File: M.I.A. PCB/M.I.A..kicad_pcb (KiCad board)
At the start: 2 copper layers, 50.8 x 101.6 mm, 118 parts, among them J1 USB_C_Receptacle_USB2.0_16P, J10 Conn_01x03, J11 Conn_01x03, J12 Conn_Coaxial, J2 Conn_01x02_Pin, J3 Conn_01x03, J4 Conn_01x03, J5 Conn_01x03, J6 Conn_01x03, J7 MSD-4-A, J8 Conn_01x03, J9 Conn_01x03, SW1 SW_Push, SW2 SW_Push, U1 W25Q128JVS, U10 INA226, U11 AMS1117-3.3, U12 AP62150WU, U13 TPS2121RUXR, U14 AP62150WU, U15 74AHC541, U16 RFM95W-915S2, U2 RP2350B-QFN80, U3 MMC5983MA, U4 ICM-42688-P, U5 MS5611-01BA, U6 TMP117xxDRV, U7 MAX-M10S, U8 KX134-1211, U9 TPS2121RUXR, Y1 ABM8-272-T3

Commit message: Started Layout
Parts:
- J7, U7: moved to B.Cu
- moved SW1 156.9 mm to (-26.5, 86.4)
- moved SW2 147.1 mm to (-16.6, 86.4)
- moved 1.1V1 138.7 mm to (3.75, 19.6)
- moved U13 106.4 mm to (36.9, 91.2)
- moved U14 98.9 mm to (36.7, 99.6)
- moved J7 98.1 mm to (-12.8, 50.6), turned to 90 degrees
- moved U5 96.5 mm to (45.5, 54.0)
- moved C24 94.7 mm to (45.5, 50.2)
- moved U9 86.1 mm to (54.3, 91.2)
- moved U12 85.6 mm to (54.1, 99.7)
- moved R1 78.0 mm to (48.1, 82.1), turned to 135 degrees
- moved C14 75.5 mm to (45.9, 80.0), turned to 135 degrees
- moved L1 75.2 mm to (49.8, 80.2), turned to -135 degrees
- moved C15 74.0 mm to (47.5, 77.8), turned to -135 degrees
- moved Y1 73.3 mm to (-15.1, 101.3), turned to 180 degrees
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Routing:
- net /QSPI_SD1: track 0.00 -> 15.7 mm, vias 0 -> 2
- net Net-(J1-CC1): track 0.00 -> 15.1 mm
- net /QSPI_SD2: track 0.00 -> 15.0 mm
- net /QSPI_SS: track 0.00 -> 14.4 mm, vias 0 -> 2
- net /D-: track 0.00 -> 11.9 mm
- net /D+: track 0.00 -> 10.8 mm
- net /USB-: track 0.00 -> 9.41 mm
- net /USB+: track 0.00 -> 8.56 mm
- net /QSPI_SD0: track 0.00 -> 8.42 mm
- net +3.3V: track 0.00 -> 7.91 mm
- net /QSPI_SCLK: track 0.00 -> 7.89 mm
- net /QSPI_SD3: track 0.00 -> 7.37 mm
- net Net-(J1-CC2): track 0.00 -> 5.99 mm
- net Net-(U2-VREG_AVDD): track 0.00 -> 5.54 mm
- net Net-(U2-VREG_LX): track 0.00 -> 5.39 mm
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- added copper zone on In1.Cu, net GND
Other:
- outline, holes or cut-outs redrawn
- copper layers 2 -> 4

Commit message: Worked on Layout, Changed IMU
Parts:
- added C14: 4.7u, Capacitor_SMD:C_0603_1608Metric, F.Cu at (89.4, 124.8)
- added C15: 4.7u, Capacitor_SMD:C_0603_1608Metric, F.Cu at (89.4, 127.3)
- added C20: 100n, Capacitor_SMD:C_0603_1608Metric, F.Cu at (79.8, 42.0)
- added C21: 100n, Capacitor_SMD:C_0603_1608Metric, F.Cu at (79.8, 44.5)
- added D3: BZT52Bxx, Diode_SMD:D_SOD-123F, F.Cu at (-0.05, 115.9)
- added D4: BZT52Bxx, Diode_SMD:D_SOD-123F, F.Cu at (-0.05, 119.3)
- added D5: BZT52Bxx, Diode_SMD:D_SOD-123F, B.Cu at (-17.7, 114.9)
- added D6: BZT52Bxx, Diode_SMD:D_SOD-123F, F.Cu at (-0.05, 126.0)
- added F1: ERBRE3R00V, JLCImport:ERBRE3R00V, F.Cu at (-0.85, 128.9)
- added F2: ERBRE3R00V, JLCImport:ERBRE3R00V, F.Cu at (-0.85, 131.3)
- added F3: ERBRE3R00V, JLCImport:ERBRE3R00V, F.Cu at (-22.3, 107.9)
- added F4: ERBRE3R00V, JLCImport:ERBRE3R00V, F.Cu at (-0.85, 136.1)
- added J13: Screw_Terminal_01x02, TerminalBlock_Phoenix:TerminalBlock_Phoenix_MKDS-1-2-3.81_1x02_P3.81mm_Horizontal, F.Cu at (67.0, 90.8)
- added J14: Screw_Terminal_01x02, TerminalBlock_Phoenix:TerminalBlock_Phoenix_MKDS-1-2-3.81_1x02_P3.81mm_Horizontal, F.Cu at (67.0, 106.0)
- added J15: Screw_Terminal_01x02, TerminalBlock_Phoenix:TerminalBlock_Phoenix_MKDS-1-2-3.81_1x02_P3.81mm_Horizontal, F.Cu at (67.0, 98.4)
- added J16: Screw_Terminal_01x02, TerminalBlock_Phoenix:TerminalBlock_Phoenix_MKDS-1-2-3.81_1x02_P3.81mm_Horizontal, F.Cu at (24.7, 81.0)
- added J17: Screw_Terminal_01x02, TerminalBlock_Phoenix:TerminalBlock_Phoenix_MKDS-1-2-3.81_1x02_P3.81mm_Horizontal, F.Cu at (24.7, 91.0)
- added J18: Screw_Terminal_01x02, TerminalBlock_Phoenix:TerminalBlock_Phoenix_MKDS-1-2-3.81_1x02_P3.81mm_Horizontal, F.Cu at (24.7, 101.0)
- added Q1: AO3400A, Package_TO_SOT_SMD:SOT-23, F.Cu at (-5.28, 116.7)
- added Q2: AO3400A, Package_TO_SOT_SMD:SOT-23, F.Cu at (-5.28, 121.3)
- added Q3: AO3400A, Package_TO_SOT_SMD:SOT-23, F.Cu at (-20.6, 114.7)
- added Q4: AO3400A, Package_TO_SOT_SMD:SOT-23, F.Cu at (-5.28, 130.5)
- added R1: 33, Resistor_SMD:R_0603_1608Metric, F.Cu at (89.4, 132.3)
- added R34: 1k, Resistor_SMD:R_0603_1608Metric, F.Cu at (-5.72, 100.5)
- added R35: 10k, Resistor_SMD:R_0603_1608Metric, F.Cu at (-5.72, 103.0)
- added R36: 5M, Resistor_SMD:R_0603_1608Metric, F.Cu at (-5.72, 105.5)
- added R37: 1M, Resistor_SMD:R_0603_1608Metric, F.Cu at (-5.72, 108.0)
- added R38: 5M, Resistor_SMD:R_0603_1608Metric, F.Cu at (-5.72, 110.5)
- added R39: 1k, Resistor_SMD:R_0603_1608Metric, F.Cu at (-5.72, 113.0)
- added R40: 10k, Resistor_SMD:R_0603_1608Metric, F.Cu at (-1.72, 100.5)
- added R41: 1M, Resistor_SMD:R_0603_1608Metric, F.Cu at (-1.72, 103.0)
- added R42: 5M, Resistor_SMD:R_0603_1608Metric, B.Cu at (-20.6, 117.9)
- added R43: 1k, Resistor_SMD:R_0603_1608Metric, B.Cu at (-17.5, 111.9)
- added R44: 10k, Resistor_SMD:R_0603_1608Metric, B.Cu at (-20.5, 111.9)
- added R45: 1M, Resistor_SMD:R_0603_1608Metric, B.Cu at (-17.6, 117.9)
- added R46: 5M, Resistor_SMD:R_0603_1608Metric, F.Cu at (2.29, 100.5)
- added R47: 1k, Resistor_SMD:R_0603_1608Metric, F.Cu at (2.29, 103.0)
- added R48: 10k, Resistor_SMD:R_0603_1608Metric, F.Cu at (2.29, 105.5)
- added R49: 1M, Resistor_SMD:R_0603_1608Metric, F.Cu at (2.29, 108.0)
- added REF**: 3x4PinHeaderCase, 3x4DupontCasing:3x4PinHeaderCase, F.Cu at (62.0, 116.5)
- added REF**: 3x4PinHeaderCase, 3x4DupontCasing:3x4PinHeaderCase, F.Cu at (28.8, 116.5)
- C28, C31, C32, C33, C34, C35, C36, C37, D1, D2, L2, L3, R11, R12, R13, R14, R15, R17, R18, R19, R20, R21, R22, R23, R24, R25, R26, R27, U12, U13, U14, U9: moved to B.Cu
- U4: value ICM-42688-P -> ICM-45686; footprint Package_LGA:LGA-14_3x2.5mm_P0.5mm_LayoutBorder3x4y -> Package_LGA:Bosch_LGA-14_3x2.5mm_P0.5mm
- moved C38 175.3 mm to (-35.2, 75.6)
- moved C39 175.3 mm to (-30.9, 85.3)
- moved R28 175.3 mm to (-35.2, 80.7)
- moved R29 175.3 mm to (-35.2, 83.2)
- moved R30 175.3 mm to (-35.2, 85.7)
- moved R31 175.3 mm to (-35.2, 88.2)
- moved R32 175.3 mm to (-35.2, 90.7)
- moved R33 175.3 mm to (-35.2, 93.2)
- moved 3v1 141.0 mm to (1.02, 1.02)
- moved 3v2 141.0 mm to (1.02, 4.08)
- moved USB_3.1 141.0 mm to (1.02, 7.12)
- moved C29 121.7 mm to (-6.85, 72.6)
- moved C30 121.7 mm to (-6.85, 75.6)
- moved R10 108.7 mm to (20.8, 71.6)
- moved R9 108.7 mm to (20.8, 69.0)
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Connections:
- U4 pad 10: +3.3V -> unconnected-(U4-RESV/AUX1_CS-Pad10)
- U4 pad 2: +3.3V -> unconnected-(U4-RESV/AUX1_SDIO/AUX1_SDI/MAS_DA-Pad2)
- U4 pad 3: +3.3V -> unconnected-(U4-RESV/AUX1_SCLK/MAS_CLK-Pad3)
- U4 pad 5: +3.3V -> Net-(U4-VDDIO)
- U4 pad 7: GND -> unconnected-(U4-RESV-Pad7)
- U4 pad 8: +3.3V -> Net-(U4-VDD)
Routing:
- net +3.3V: track 7.91 -> 66.5 mm, vias 0 -> 8
- net +1V1: track 0.82 -> 17.6 mm, vias 1 -> 2
- net Net-(U2-XIN): track 0.00 -> 12.5 mm
- net GND: track 3.20 -> 12.8 mm, vias 7 -> 11
- net Net-(U2-XOUT): track 0.00 -> 7.61 mm
- net Net-(C19-Pad2): track 0.00 -> 3.64 mm
- net unconnected-(U2-GPIO1-Pad78): track 0.00 -> 1.87 mm, vias 0 -> 1
- net unconnected-(U2-GPIO0-Pad77): track 0.00 -> 1.39 mm, vias 0 -> 1
- net unconnected-(U2-GPIO2-Pad79): track 0.00 -> 1.39 mm, vias 0 -> 1
- net unconnected-(U2-GPIO3-Pad80): track 0.00 -> 0.37 mm, vias 0 -> 1
- added copper zone on In2.Cu, net +3.3V
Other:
- board size 50.8 x 101.6 mm -> 50.8 x 106.6 mm
- copper layers 4 -> 6
- board text added: "|\/||/\"

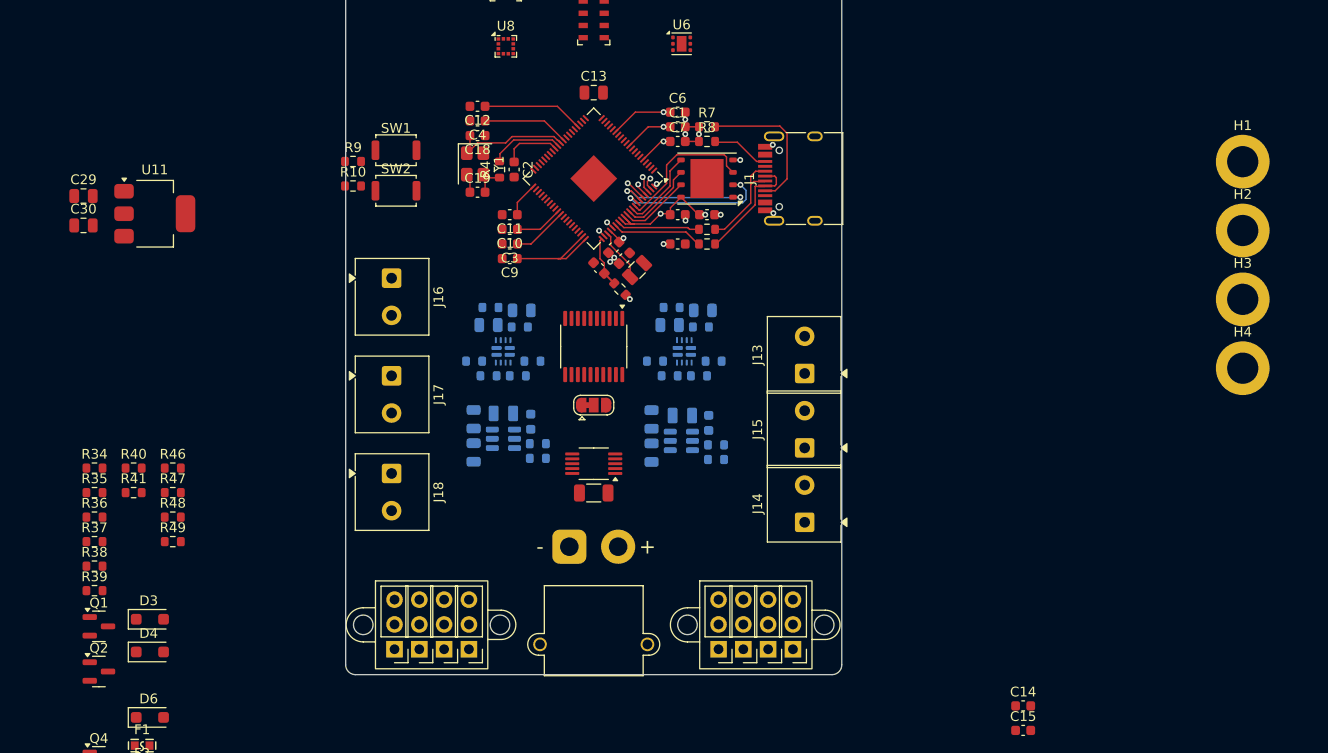
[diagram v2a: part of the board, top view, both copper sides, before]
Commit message: added servo pin protector and changed screw terminal size
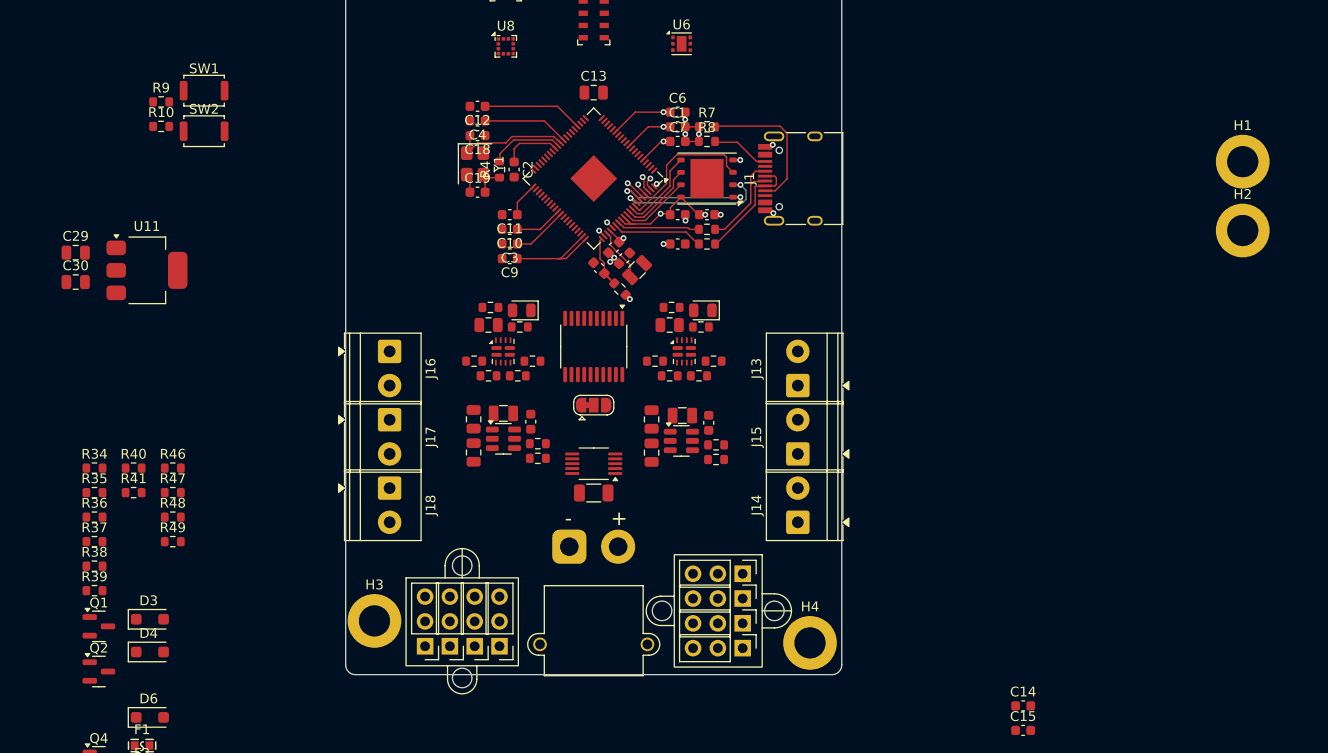
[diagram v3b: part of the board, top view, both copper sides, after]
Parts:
- C28, C31, C32, C33, C34, C35, C36, C37, D1, D2, L2, L3, R11, R12, R13, R14, R15, R17, R18, R19, R20, R21, R22, R23, R24, R25, R26, R27, U12, U13, U14, U9: moved to F.Cu
- J13, J14, J15, J16, J17, J18: footprint TerminalBlock_Phoenix:TerminalBlock_Phoenix_MKDS-1-2-3.81_1x02_P3.81mm_Horizontal -> TerminalBlock_Phoenix:TerminalBlock_Phoenix_PT-1,5-2-3.5-H_1x02_P3.50mm_Horizontal
- REF** (x2): value 3x4PinHeaderCase -> 3x4PinHeaderCase90deg; footprint 3x4DupontCasing:3x4PinHeaderCase -> 3x4DupontCasing:3x4PinHeaderCase90deg
- moved H3 94.8 mm to (22.9, 116.1)
- moved H4 52.5 mm to (67.5, 118.3)
- moved R10 20.6 mm to (1.10, 65.5)
- moved SW1 20.6 mm to (5.50, 61.8)
- moved R9 20.6 mm to (1.10, 63.0)
- moved SW2 20.6 mm to (5.50, 66.0)
- moved J3 9.29 mm to (60.6, 111.3), turned to -90 degrees
- moved J16 7.50 mm to (24.5, 88.5)
- moved C30 5.85 mm to (-7.65, 81.4)
- moved C29 5.85 mm to (-7.65, 78.4)
- moved U11 5.85 mm to (-0.35, 80.2)
- moved J5 5.81 mm to (60.6, 113.8), turned to -90 degrees
- moved J17 4.50 mm to (24.5, 95.5)
- moved REF** 4.11 mm to (58.1, 115.1), turned to -90 degrees
- moved J4 3.15 mm to (35.8, 118.7)
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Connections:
- J2 pad 1: VBAT -> GND
- J2 pad 2: GND -> VBAT

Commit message: updated LDO and Power Sensor
may need to change LDO to support power draw of RFM95CW
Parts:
- removed U10: INA226, Package_SO:VSSOP-10_3x3mm_P0.5mm
- added U11: INA219AxDCN, Package_TO_SOT_SMD:SOT-23-8, F.Cu at (45.4, 100.0)
- added U17: TLV70233_SOT23-5, Package_TO_SOT_SMD:SOT-23-5, F.Cu at (-11.2, 57.1)
- C29, C30: value 10u -> 1u; moved to B.Cu
- U11: moved to B.Cu
- moved U11 29.2 mm to (-2.75, 51.0), turned to 180 degrees
- moved C30 28.5 mm to (-10.7, 53.1), turned to 180 degrees
- moved C29 28.5 mm to (-10.7, 50.1), turned to 180 degrees
- turned J7 to 90 degrees
- turned R16 to 0 degrees
